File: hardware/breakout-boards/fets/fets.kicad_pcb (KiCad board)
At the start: 2 copper layers, 50.5 x 48.8 mm, 39 parts, among them P1 CONN_01X06, P2 CONN_01X06, P3 CONN_01X03, P4 CONN_01X02, Q1 IRF7530, Q2 IRF7530, Q3 IRF7530, Q4 IRF7530, Q5 IRF7530, Q6 IRF7530

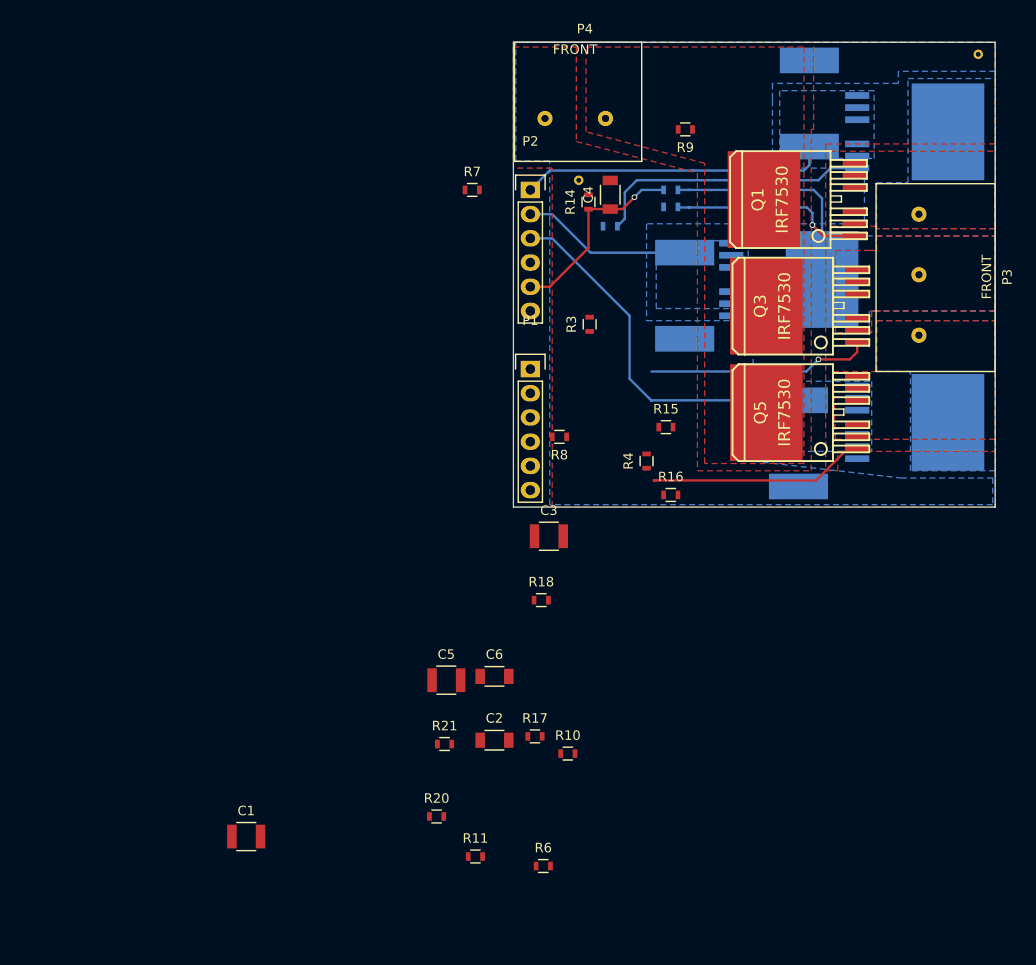
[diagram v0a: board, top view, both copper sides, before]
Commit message: FET breakoutboard complete, generated gerbers and sent off to fab
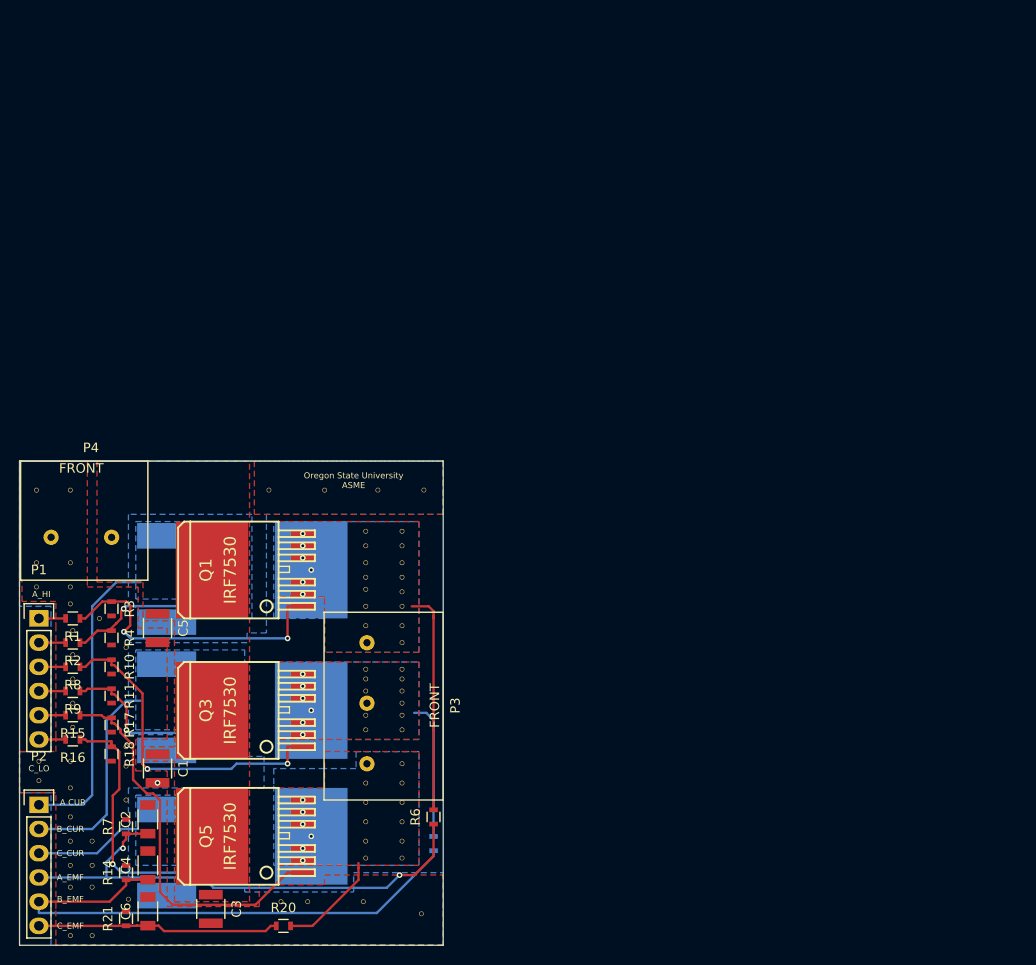
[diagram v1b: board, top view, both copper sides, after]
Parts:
- removed REF** (x2): hack-via, fet-libs:hack-via
- added T1: hack-via, fet-libs:hack-via, F.Cu at (167.1, 85.1)
- added T1: hack-via, fet-libs:hack-via, F.Cu at (167.1, 86.9)
- added T1: hack-via, fet-libs:hack-via, F.Cu at (167.1, 88.4)
- added T1: hack-via, fet-libs:hack-via, F.Cu at (167.1, 89.9)
- added T1: hack-via, fet-libs:hack-via, F.Cu at (167.1, 91.4)
- added T1: hack-via, fet-libs:hack-via, F.Cu at (167.1, 93.5)
- added T1: hack-via, fet-libs:hack-via, F.Cu at (167.1, 95.2)
- added T1: hack-via, fet-libs:hack-via, F.Cu at (163.3, 100.3)
- added T1: hack-via, fet-libs:hack-via, F.Cu at (163.3, 99.1)
- added T1: hack-via, fet-libs:hack-via, F.Cu at (163.3, 98.0)
- added T1: hack-via, fet-libs:hack-via, F.Cu at (167.1, 98.0)
- added T1: hack-via, fet-libs:hack-via, F.Cu at (167.1, 83.6)
- added T1: hack-via, fet-libs:hack-via, F.Cu at (167.1, 99.1)
- added T1: hack-via, fet-libs:hack-via, F.Cu at (167.1, 100.3)
- added T1: hack-via, fet-libs:hack-via, F.Cu at (167.1, 101.6)
- added T1: hack-via, fet-libs:hack-via, F.Cu at (167.1, 102.9)
- added T1: hack-via, fet-libs:hack-via, F.Cu at (163.3, 102.9)
- added T1: hack-via, fet-libs:hack-via, F.Cu at (163.3, 104.4)
- added T1: hack-via, fet-libs:hack-via, F.Cu at (167.1, 104.4)
- added T1: hack-via, fet-libs:hack-via, F.Cu at (167.1, 114.0)
- added T1: hack-via, fet-libs:hack-via, F.Cu at (167.1, 116.1)
- added T1: hack-via, fet-libs:hack-via, F.Cu at (167.1, 117.9)
- added T1: hack-via, fet-libs:hack-via, F.Cu at (163.3, 83.6)
- added T1: hack-via, fet-libs:hack-via, F.Cu at (163.3, 117.9)
- added T1: hack-via, fet-libs:hack-via, F.Cu at (163.3, 116.1)
- added T1: hack-via, fet-libs:hack-via, F.Cu at (163.3, 114.0)
- added T1: hack-via, fet-libs:hack-via, F.Cu at (167.1, 112.0)
- added T1: hack-via, fet-libs:hack-via, F.Cu at (163.3, 112.0)
- added T1: hack-via, fet-libs:hack-via, F.Cu at (163.3, 110.0)
- added T1: hack-via, fet-libs:hack-via, F.Cu at (167.1, 110.0)
- added T1: hack-via, fet-libs:hack-via, F.Cu at (167.1, 108.0)
- added T1: hack-via, fet-libs:hack-via, F.Cu at (138.2, 111.8)
- added T1: hack-via, fet-libs:hack-via, F.Cu at (138.2, 95.8)
- added T1: hack-via, fet-libs:hack-via, F.Cu at (163.3, 85.1)
- added T1: hack-via, fet-libs:hack-via, F.Cu at (132.6, 94.0)
- added T1: hack-via, fet-libs:hack-via, F.Cu at (132.6, 96.5)
- added T1: hack-via, fet-libs:hack-via, F.Cu at (132.6, 99.1)
- added T1: hack-via, fet-libs:hack-via, F.Cu at (132.6, 101.6)
- added T1: hack-via, fet-libs:hack-via, F.Cu at (132.6, 104.1)
- added T1: hack-via, fet-libs:hack-via, F.Cu at (135.4, 92.7)
- added T1: hack-via, fet-libs:hack-via, F.Cu at (132.3, 79.2)
- added T1: hack-via, fet-libs:hack-via, F.Cu at (128.8, 79.2)
- added T1: hack-via, fet-libs:hack-via, F.Cu at (159.0, 79.2)
- added T1: hack-via, fet-libs:hack-via, F.Cu at (164.6, 79.2)
- added T1: hack-via, fet-libs:hack-via, F.Cu at (163.3, 86.9)
- added T1: hack-via, fet-libs:hack-via, F.Cu at (169.4, 79.2)
- added T1: hack-via, fet-libs:hack-via, F.Cu at (153.2, 79.2)
- added T1: hack-via, fet-libs:hack-via, F.Cu at (138.2, 106.2)
- added T1: hack-via, fet-libs:hack-via, F.Cu at (138.2, 108.2)
- added T1: hack-via, fet-libs:hack-via, F.Cu at (129.0, 109.7)
- added T1: hack-via, fet-libs:hack-via, F.Cu at (129.0, 107.7)
- added T1: hack-via, fet-libs:hack-via, F.Cu at (132.3, 107.7)
- added T1: hack-via, fet-libs:hack-via, F.Cu at (132.3, 110.5)
- added T1: hack-via, fet-libs:hack-via, F.Cu at (132.3, 120.9)
- added T1: hack-via, fet-libs:hack-via, F.Cu at (134.6, 120.9)
- added T1: hack-via, fet-libs:hack-via, F.Cu at (163.3, 88.4)
- added T1: hack-via, fet-libs:hack-via, F.Cu at (134.6, 116.1)
- added T1: hack-via, fet-libs:hack-via, F.Cu at (132.3, 116.1)
- added T1: hack-via, fet-libs:hack-via, F.Cu at (154.4, 122.4)
- added T1: hack-via, fet-libs:hack-via, F.Cu at (157.2, 122.4)
- added T1: hack-via, fet-libs:hack-via, F.Cu at (163.1, 122.4)
- added T1: hack-via, fet-libs:hack-via, F.Cu at (169.2, 123.7)
- added T1: hack-via, fet-libs:hack-via, F.Cu at (132.3, 126.0)
- added T1: hack-via, fet-libs:hack-via, F.Cu at (138.4, 122.2)
- added T1: hack-via, fet-libs:hack-via, F.Cu at (134.6, 126.0)
- added T1: hack-via, fet-libs:hack-via, F.Cu at (132.3, 113.5)
- added T1: hack-via, fet-libs:hack-via, F.Cu at (163.3, 89.7)
- added T1: hack-via, fet-libs:hack-via, F.Cu at (134.6, 118.6)
- added T1: hack-via, fet-libs:hack-via, F.Cu at (132.3, 118.6)
- added T1: hack-via, fet-libs:hack-via, F.Cu at (132.3, 91.2)
- added T1: hack-via, fet-libs:hack-via, F.Cu at (128.8, 89.4)
- added T1: hack-via, fet-libs:hack-via, F.Cu at (132.3, 89.4)
- added T1: hack-via, fet-libs:hack-via, F.Cu at (132.3, 86.9)
- added T1: hack-via, fet-libs:hack-via, F.Cu at (128.8, 86.9)
- added T1: hack-via, fet-libs:hack-via, F.Cu at (163.3, 91.4)
- added T1: hack-via, fet-libs:hack-via, F.Cu at (163.3, 93.5)
- R1, R2: moved to F.Cu
- moved R9 87.2 mm to (132.6, 100.3)
- moved C4 85.5 mm to (140.5, 118.6)
- moved R14 85.5 mm to (138.2, 119.4)
- moved P2 82.6 mm to (129.0, 112.3)
- moved Q2 81.1 mm to (148.1, 87.6)
- moved Q6 79.7 mm to (148.1, 115.6)
- moved R19 79.0 mm to (145.0, 112.3)
- moved R1 76.2 mm to (132.6, 92.7)
- moved R7 76.0 mm to (138.2, 114.6), turned to 90 degrees
- moved R5 73.9 mm to (145.0, 83.6), turned to 270 degrees
- moved P3 73.3 mm to (171.4, 111.8)
- moved Q5 73.2 mm to (156.7, 115.6)
- moved R13 73.0 mm to (170.4, 116.3), turned to 90 degrees
- moved Q3 72.0 mm to (156.7, 102.4)
- moved R2 71.3 mm to (132.6, 95.2)
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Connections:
- net Net-(Q1-Pad1) renamed /A_HI_G
- net Net-(Q2-Pad1) renamed /A_LO_G
- net Net-(Q3-Pad1) renamed /B_HI_G
- net Net-(Q4-Pad1) renamed /B_LO_G
- net Net-(Q5-Pad1) renamed /C_HI_G
- net Net-(Q6-Pad1) renamed /C_LO_G
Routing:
- net A_EMF: track 0.00 -> 54.5 mm, vias 0 -> 2
- net B_EMF: track 20.6 -> 58.4 mm, vias 1 -> 0
- net MOTOR_A: track 0.00 -> 37.0 mm, vias 0 -> 6
- net /C_LO_G: track 0.00 -> 28.9 mm, vias 0 -> 1
- net C_CUR: track 39.1 -> 11.5 mm
- net C_EMF: track 0.00 -> 25.4 mm
- net MOTOR_C: track 0.00 -> 24.3 mm, vias 0 -> 6
- net /B_LO_G: track 0.00 -> 19.4 mm, vias 0 -> 1
- net /C_HI_G: track 23.0 -> 41.3 mm
- net /A_LO_G: track 29.3 -> 17.4 mm, vias 0 -> 1
- net /B_HI_G: track 23.4 -> 35.1 mm, vias 1 -> 2
- net /A_HI_G: track 21.1 -> 31.6 mm, vias 1 -> 2
- net B_CUR: track 17.9 -> 22.0 mm
- net MOTOR_B: track 24.3 -> 27.9 mm, vias 0 -> 6
- net C_LO: track 0.00 -> 2.81 mm
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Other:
- board size 50.5 x 48.8 mm -> 44.4 x 50.8 mm
- rule via_min_drill: 0.3 -> 0.3302
- board text added: "A CUR"
- board text added: "A_EMF"
- board text added: "A_HI"
- board text added: "B_CUR"
- board text added: "B_EMF"
- board text added: "C_CUR"
- board text added: "C_EMF"
- board text added: "C_LO"
- board text added: "Oregon State University ASME"
